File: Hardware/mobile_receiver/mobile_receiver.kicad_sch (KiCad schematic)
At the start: 32 parts, among them J1 Conn_02x07_Top_Bottom, SW1 SW_SPST, SW2 SW_Push, SW3 SW_Push, SW4 SW_Push, SW5 SW_Push, SW6 SW_Push, SW7 SW_Push, U2 kb2040

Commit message: Fixed USB traces, radio connectors, finished UART adapter
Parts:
- added C3: 10uF, Capacitor_SMD:C_1210_3225Metric, symbol Device:C
- R4, R5: value 60Ω -> 10K
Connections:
- net +3.3V: now also C3.2
- net GND: now also C3.1
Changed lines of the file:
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@@
 	)
 	(junction
+		(at 111.76 158.75)
+		(diameter 0)
+		(color 0 0 0 0)
+	)
+	(junction
 		(at 236.22 86.36)
 		(diameter 0)
@@
 	(wire
 		(pts
+			(xy 111.76 158.75) (xy 124.46 158.75)
+		)
+		(stroke
+			(width 0)
+			(type default)
+		)
+	)
+	(wire
+		(pts
 			(xy 43.18 167.64) (xy 43.18 176.53)
 		)
@@
 	(wire
 		(pts
+			(xy 109.22 154.94) (xy 111.76 154.94)
+		)
+		(stroke
+			(width 0)
+			(type default)
+		)
+	)
+	(wire
+		(pts
 			(xy 119.38 78.74) (xy 132.08 78.74)
 		)
@@
 	(wire
 		(pts
+			(xy 104.14 147.32) (xy 109.22 147.32)
+		)
+		(stroke
+			(width 0)
+			(type default)
+		)
+	)
+	(wire
+		(pts
 			(xy 264.16 41.91) (xy 264.16 45.72)
 		)
@@
 	(wire
 		(pts
-			(xy 110.49 158.75) (xy 124.46 158.75)
+			(xy 110.49 158.75) (xy 111.76 158.75)
 		)
 		(stroke
@@
 	(wire
 		(pts
+			(xy 111.76 154.94) (xy 111.76 158.75)
+		)
+		(stroke
+			(width 0)
+			(type default)
+		)
+	)
+	(wire
+		(pts
 			(xy 262.89 41.91) (xy 264.16 41.91)
 		)
@@
 			)
 		)
-		(property "Value" "60Ω"
+		(property "Value" "10K"
 			(at 104.14 176.5299 0)
 			(effects
@@
 	)
 	(symbol
+		(lib_id "power:GND")
+		(at 104.14 147.32 270)
+		(unit 1)
+		(exclude_from_sim no)
+		(in_bom yes)
+		(on_board yes)
+		(dnp no)
+		(property "Reference" "#PWR019"
+			(at 97.79 147.32 0)
+			(effects
+				(font
+					(size 1.27 1.27)
+				)
+				(hide yes)
+			)
+		)
+		(property "Value" "GND"
+			(at 101.092 147.32 90)
+			(effects
+				(font
+					(size 1.27 1.27)
+				)
+				(justify right)
+			)
+		)
+		(property "Footprint" ""
+			(at 104.14 147.32 0)
+			(effects
+				(font
+					(size 1.27 1.27)
+				)
+				(hide yes)
+			)
+		)
+		(property "Datasheet" ""
+			(at 104.14 147.32 0)
+			(effects
+				(font
+					(size 1.27 1.27)
+				)
+				(hide yes)
+			)
+		)
+		(property "Description" "Power symbol creates a global label with name \"GND\" , ground"
+			(at 104.14 147.32 0)
+			(effects
+				(font
+					(size 1.27 1.27)
+				)
+				(hide yes)
+			)
+		)
+		(pin "1"
+		)
+		(instances
+			(project "mobile_receiver"
+				(path "/027e157c-a777-4d43-93ce-409e4d09b50d"
+					(reference "#PWR019")
+					(unit 1)
+				)
+			)
+		)
+	)
+	(symbol
 		(lib_id "Device:R")
 		(at 203.2 102.87 180)
@@
 	)
 	(symbol
+		(lib_id "Device:C")
+		(at 109.22 151.13 0)
+		(unit 1)
+		(exclude_from_sim no)
+		(in_bom yes)
+		(on_board yes)
+		(dnp no)
+		(fields_autoplaced yes)
+		(property "Reference" "C3"
+			(at 113.03 149.8599 0)
+			(effects
+				(font
+					(size 1.27 1.27)
+				)
+				(justify left)
+			)
+		)
+		(property "Value" "10uF"
+			(at 113.03 152.3999 0)
+			(effects
+				(font
+					(size 1.27 1.27)
+				)
+				(justify left)
+			)
+		)
+		(property "Footprint" "Capacitor_SMD:C_1210_3225Metric"
+			(at 110.1852 154.94 0)
+			(effects
+				(font
+					(size 1.27 1.27)
+				)
+				(hide yes)
+			)
+		)
+		(property "Datasheet" "~"
+			(at 109.22 151.13 0)
+			(effects
+				(font
+					(size 1.27 1.27)
+				)
+				(hide yes)
+			)
+		)
+		(property "Description" "Unpolarized capacitor"
+			(at 109.22 151.13 0)
+			(effects
+				(font
+					(size 1.27 1.27)
+				)
+				(hide yes)
+			)
+		)
+		(pin "1"
+		)
+		(pin "2"
+		)
+		(instances
+			(project "mobile_receiver"
+				(path "/027e157c-a777-4d43-93ce-409e4d09b50d"
+					(reference "C3")
+					(unit 1)
+				)
+			)
+		)
+	)
+	(symbol
 		(lib_id "power:GND")
 		(at 81.28 78.74 180)
@@
 			)
 		)
-		(property "Value" "60Ω"
+		(property "Value" "10K"
 			(at 95.25 175.2599 0)
 			(effects

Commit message: Added new Switch
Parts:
- SW1: footprint Button_Switch_SMD:SW_SPDT_PCM12 -> My footprints:OS102011MA1QN1_CNK
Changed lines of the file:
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@@
 			)
 		)
-		(property "Footprint" "Button_Switch_SMD:SW_SPDT_PCM12"
+		(property "Footprint" "My footprints:OS102011MA1QN1_CNK"
 			(at 69.85 39.37 0)
 			(effects

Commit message: Updated package sizes
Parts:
- C3, C6: footprint Capacitor_SMD:C_1210_3225Metric -> Capacitor_SMD:C_0805_2012Metric_Pad1.18x1.45mm_HandSolder
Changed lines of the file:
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@@
 			)
 		)
-		(property "Footprint" "Capacitor_SMD:C_1210_3225Metric"
+		(property "Footprint" "Capacitor_SMD:C_0805_2012Metric_Pad1.18x1.45mm_HandSolder"
 			(at 51.7652 43.18 0)
 			(effects
@@
 			)
 		)
-		(property "Footprint" "Capacitor_SMD:C_1210_3225Metric"
+		(property "Footprint" "Capacitor_SMD:C_0805_2012Metric_Pad1.18x1.45mm_HandSolder"
 			(at 110.1852 154.94 0)
 			(effects

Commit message: Tactile Buttons Replaced
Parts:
- SW2, SW3, SW4, SW5, SW6, SW7: footprint Button_Switch_SMD:SW_Push_1TS009xxxx-xxxx-xxxx_6x6x5mm -> Button_Switch_SMD:SW_Push_1P1T_NO_E-Switch_TL3301NxxxxxG
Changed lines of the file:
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@@
 			)
 		)
-		(property "Footprint" "Button_Switch_SMD:SW_Push_1TS009xxxx-xxxx-xxxx_6x6x5mm"
+		(property "Footprint" "Button_Switch_SMD:SW_Push_1P1T_NO_E-Switch_TL3301NxxxxxG"
 			(at 218.44 69.85 0)
 			(effects
@@
 			)
 		)
-		(property "Footprint" "Button_Switch_SMD:SW_Push_1TS009xxxx-xxxx-xxxx_6x6x5mm"
+		(property "Footprint" "Button_Switch_SMD:SW_Push_1P1T_NO_E-Switch_TL3301NxxxxxG"
 			(at 218.44 107.95 0)
 			(effects
@@
 			)
 		)
-		(property "Footprint" "Button_Switch_SMD:SW_Push_1TS009xxxx-xxxx-xxxx_6x6x5mm"
+		(property "Footprint" "Button_Switch_SMD:SW_Push_1P1T_NO_E-Switch_TL3301NxxxxxG"
 			(at 218.44 50.8 0)
 			(effects
@@
 			)
 		)
-		(property "Footprint" "Button_Switch_SMD:SW_Push_1TS009xxxx-xxxx-xxxx_6x6x5mm"
+		(property "Footprint" "Button_Switch_SMD:SW_Push_1P1T_NO_E-Switch_TL3301NxxxxxG"
 			(at 257.81 133.35 0)
 			(effects
@@
 			)
 		)
-		(property "Footprint" "Button_Switch_SMD:SW_Push_1TS009xxxx-xxxx-xxxx_6x6x5mm"
+		(property "Footprint" "Button_Switch_SMD:SW_Push_1P1T_NO_E-Switch_TL3301NxxxxxG"
 			(at 218.44 87.63 0)
 			(effects
@@
 			)
 		)
-		(property "Footprint" "Button_Switch_SMD:SW_Push_1TS009xxxx-xxxx-xxxx_6x6x5mm"
+		(property "Footprint" "Button_Switch_SMD:SW_Push_1P1T_NO_E-Switch_TL3301NxxxxxG"
 			(at 257.81 36.83 0)
 			(effects

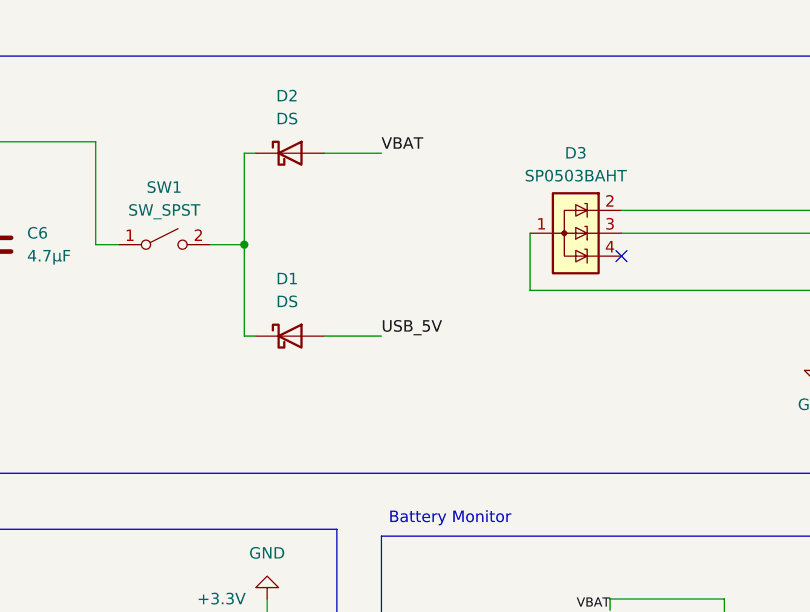
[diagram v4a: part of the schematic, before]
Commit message: Fixed RF trace, Added new Diodes, better power traces and new switches
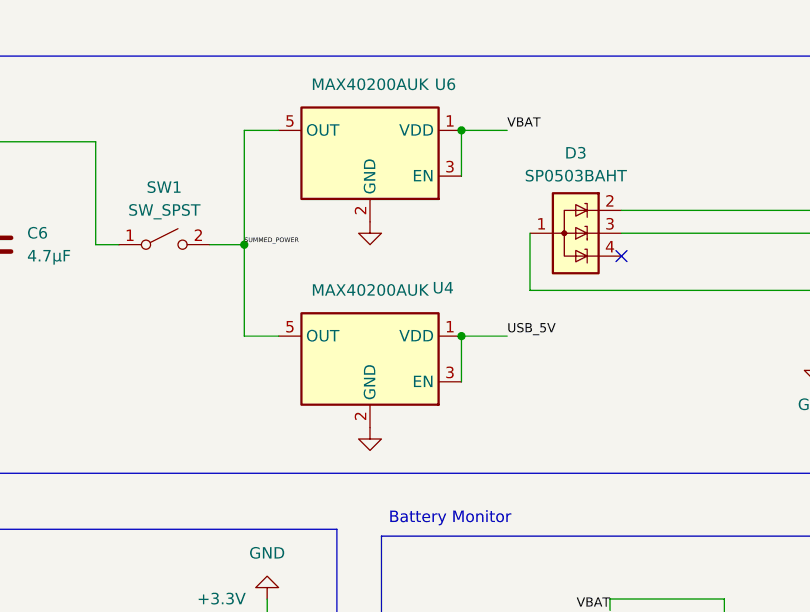
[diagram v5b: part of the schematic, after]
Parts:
- removed D1, D2: DS, Diode_SMD:D_SOD-123F, symbol Device:D_Schottky
- added U4, U6: MAX40200AUK, Package_TO_SOT_SMD:SOT-23-5, symbol Analog_Switch:MAX40200AUK
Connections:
- net GND: now also U4.2 (GND), U6.2 (GND)
- net USB_5V: now also U4.1 (VDD), U4.3 (EN)
- net VBAT: now also U6.1 (VDD), U6.3 (EN)
- net SUMMED_POWER: now reaches SW1.2 (B)
- net SUMMED_POWER: now also U4.5 (OUT), U6.5 (OUT)

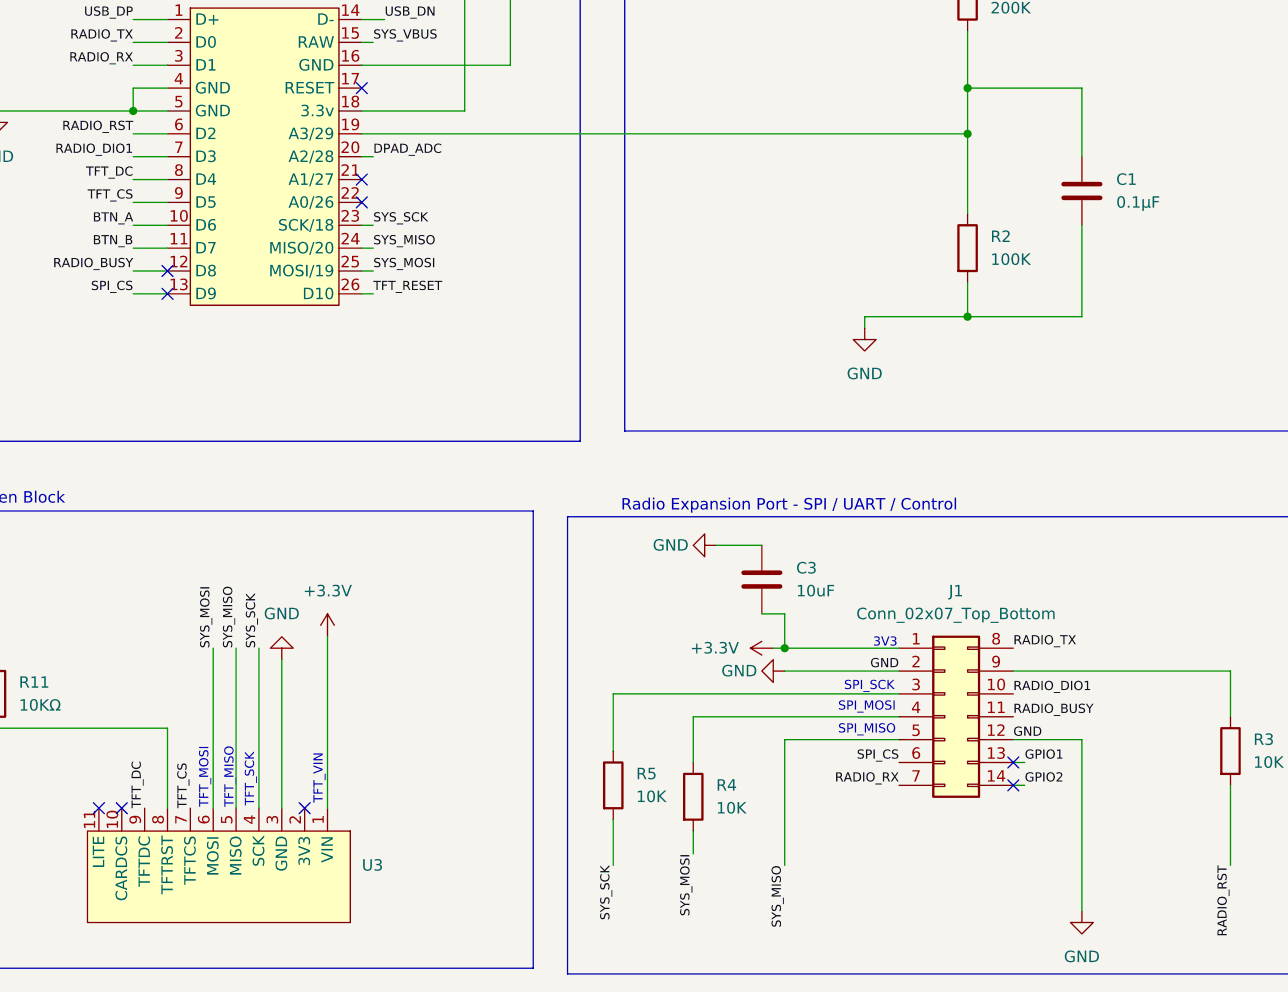
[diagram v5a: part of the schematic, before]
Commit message: SPI resistors removed and transmission added
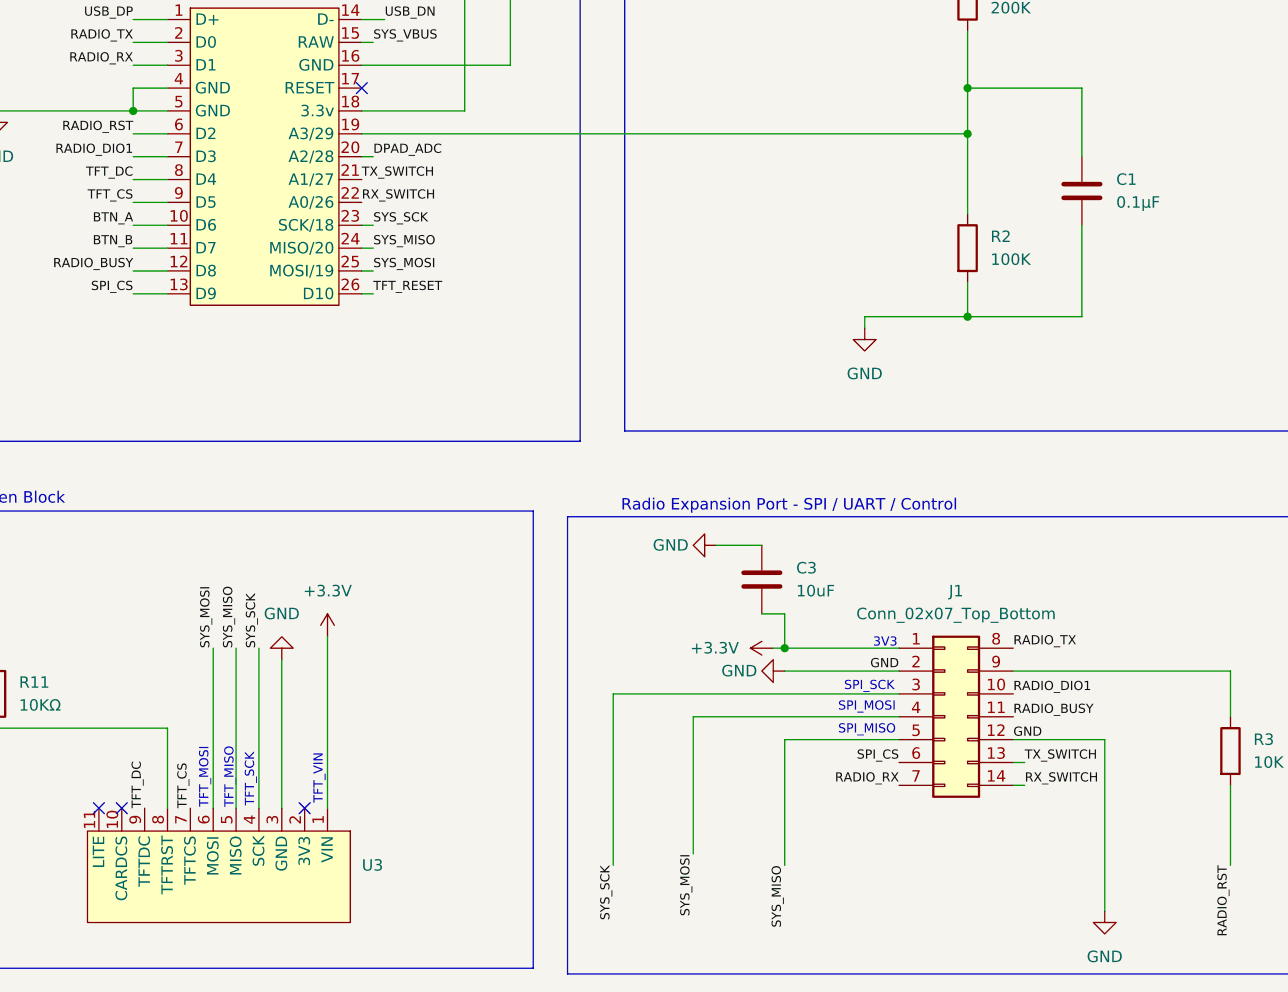
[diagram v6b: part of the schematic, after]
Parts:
- removed R4, R5: 10K, Resistor_SMD:R_0805_2012Metric_Pad1.20x1.40mm_HandSolder, symbol Device:R
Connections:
- net GPIO1 is gone; now on net TX_SWITCH: J1.13 (Pin_13)
- net GPIO2 is gone; now on net RX_SWITCH: J1.14 (Pin_14)
- net SYS_MOSI: now also J1.4 (Pin_4)
- net SYS_SCK: now also J1.3 (Pin_3)
- net TX_SWITCH: now reaches U2.21 (A1/27)
- net RX_SWITCH: now reaches U2.22 (A0/26)
- no-connect marks 11 -> 5
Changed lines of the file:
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@@
 	)
 	(no_connect
-		(at 137.16 171.45)
-	)
-	(no_connect
 		(at 35.56 176.53)
 	)
 	(no_connect
-		(at 64.77 109.22)
-	)
-	(no_connect
-		(at 137.16 173.99)
-	)
-	(no_connect
-		(at 43.18 119.38)
-	)
-	(no_connect
 		(at 58.42 176.53)
 	)
@@
 		(at 64.77 96.52)
 	)
-	(no_connect
-		(at 43.18 116.84)
-	)
-	(no_connect
-		(at 64.77 106.68)
-	)
 	(wire
 		(pts
@@
 	(wire
 		(pts
-			(xy 92.71 163.83) (xy 92.71 170.18)
+			(xy 92.71 163.83) (xy 92.71 182.88)
 		)
 		(stroke
@@
 	(wire
 		(pts
-			(xy 144.78 187.96) (xy 144.78 168.91)
+			(xy 147.32 187.96) (xy 147.32 168.91)
 		)
 		(stroke
@@
 	(wire
 		(pts
-			(xy 120.65 35.56) (xy 151.13 35.56)
+			(xy 137.16 171.45) (xy 138.43 171.45)
 		)
 		(stroke
@@
 	(wire
 		(pts
-			(xy 101.6 179.07) (xy 101.6 181.61)
+			(xy 120.65 35.56) (xy 151.13 35.56)
 		)
 		(stroke
@@
 	(wire
 		(pts
-			(xy 92.71 177.8) (xy 92.71 182.88)
-		)
-		(stroke
-			(width 0)
-			(type default)
-		)
-	)
-	(wire
-		(pts
-			(xy 144.78 168.91) (xy 137.16 168.91)
+			(xy 147.32 168.91) (xy 137.16 168.91)
 		)
 		(stroke
@@
 	(wire
 		(pts
-			(xy 138.43 171.45) (xy 137.16 171.45)
-		)
-		(stroke
-			(width 0)
-			(type default)
-		)
-	)
-	(wire
-		(pts
 			(xy 149.86 31.75) (xy 151.13 31.75)
 		)
@@
 	(wire
 		(pts
-			(xy 101.6 166.37) (xy 101.6 171.45)
+			(xy 101.6 166.37) (xy 101.6 181.61)
 		)
 		(stroke
@@
 		)
 	)
+	(label "TX_SWITCH"
+		(at 64.77 106.68 0)
+		(effects
+			(font
+				(size 1.016 1.016)
+			)
+			(justify left bottom)
+		)
+	)
 	(label "SYS_MISO"
 		(at 111.76 182.88 270)
@@
 		)
 	)
+	(label "RX_SWITCH"
+		(at 64.77 109.22 0)
+		(effects
+			(font
+				(size 1.016 1.016)
+			)
+			(justify left bottom)
+		)
+	)
 	(label "USB_5V"
 		(at 149.86 31.75 180)
@@
 		)
 	)
-	(label "GPIO1"
+	(label "TX_SWITCH"
 		(at 138.43 171.45 0)
 		(effects
@@
 		)
 	)
-	(label "GPIO2"
+	(label "RX_SWITCH"
 		(at 138.43 173.99 0)
 		(effects
@@
 	)
 	(symbol
-		(lib_id "Device:R")
-		(at 101.6 175.26 0)
-		(unit 1)
-		(exclude_from_sim no)
-		(in_bom yes)
-		(on_board yes)
-		(dnp no)
-		(fields_autoplaced yes)
-		(property "Reference" "R4"
-			(at 104.14 173.9899 0)
-			(effects
-				(font
-					(size 1.27 1.27)
-				)
-				(justify left)
-			)
-		)
-		(property "Value" "10K"
-			(at 104.14 176.5299 0)
-			(effects
-				(font
-					(size 1.27 1.27)
-				)
-				(justify left)
-			)
-		)
-		(property "Footprint" "Resistor_SMD:R_0805_2012Metric_Pad1.20x1.40mm_HandSolder"
-			(at 99.822 175.26 90)
-			(effects
-				(font
-					(size 1.27 1.27)
-				)
-				(hide yes)
-			)
-		)
-		(property "Datasheet" "~"
-			(at 101.6 175.26 0)
-			(effects
-				(font
-					(size 1.27 1.27)
-				)
-				(hide yes)
-			)
-		)
-		(property "Description" "Resistor"
-			(at 101.6 175.26 0)
-			(effects
-				(font
-					(size 1.27 1.27)
-				)
-				(hide yes)
-			)
-		)
-		(pin "1"
-		)
-		(pin "2"
-		)
-		(instances
-			(project "mobile_receiver"
-				(path "/027e157c-a777-4d43-93ce-409e4d09b50d"
-					(reference "R4")
-					(unit 1)
-				)
-			)
-		)
-	)
-	(symbol
 		(lib_id "Switch:SW_Push")
 		(at 218.44 74.93 0)
@@
 	(symbol
 		(lib_id "power:GND")
-		(at 144.78 187.96 0)
+		(at 147.32 187.96 0)
 		(unit 1)
 		(exclude_from_sim no)
@@
 		(fields_autoplaced yes)
 		(property "Reference" "#PWR09"
-			(at 144.78 194.31 0)
+			(at 147.32 194.31 0)
 			(effects
 				(font
@@
 		)
 		(property "Value" "GND"
-			(at 144.78 193.04 0)
+			(at 147.32 193.04 0)
 			(effects
 				(font
@@
 		)
 		(property "Footprint" ""
-			(at 144.78 187.96 0)
+			(at 147.32 187.96 0)
 			(effects
 				(font
@@
 		)
 		(property "Datasheet" ""
-			(at 144.78 187.96 0)
+			(at 147.32 187.96 0)
 			(effects
 				(font
@@
 		)
 		(property "Description" "Power symbol creates a global label with name \"GND\" , ground"
-			(at 144.78 187.96 0)
+			(at 147.32 187.96 0)
 			(effects
 				(font
@@
 					(unit 1)
 				)
-			)
-		)
-	)
-	(symbol
-		(lib_id "Device:R")
-		(at 92.71 173.99 0)
-		(unit 1)
-		(exclude_from_sim no)
-		(in_bom yes)
-		(on_board yes)
-		(dnp no)
-		(fields_autoplaced yes)
-		(property "Reference" "R5"
-			(at 95.25 172.7199 0)
-			(effects
-				(font
-					(size 1.27 1.27)
-				)
-				(justify left)
-			)
-		)
-		(property "Value" "10K"
-			(at 95.25 175.2599 0)
-			(effects
-				(font
-					(size 1.27 1.27)
-				)
-				(justify left)
-			)
-		)
-		(property "Footprint" "Resistor_SMD:R_0805_2012Metric_Pad1.20x1.40mm_HandSolder"
-			(at 90.932 173.99 90)
-			(effects
-				(font
-					(size 1.27 1.27)
-				)
-				(hide yes)
-			)
-		)
-		(property "Datasheet" "~"
-			(at 92.71 173.99 0)
-			(effects
-				(font
-					(size 1.27 1.27)
-				)
-				(hide yes)
-			)
-		)
-		(property "Description" "Resistor"
-			(at 92.71 173.99 0)
-			(effects
-				(font
-					(size 1.27 1.27)
-				)
-				(hide yes)
-			)
-		)
-		(pin "1"
-		)
-		(pin "2"
-		)
-		(instances
-			(project "mobile_receiver"
-				(path "/027e157c-a777-4d43-93ce-409e4d09b50d"
-					(reference "R5")
-					(unit 1)
-				)
